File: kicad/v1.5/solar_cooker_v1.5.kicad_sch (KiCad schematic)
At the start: 18 parts, among them U10 GPS, U2 microSD, U3 clock_module, U5 anemometer, U6 BME680, U6 PT100, U7 pyranometer, U8 PT100, U9 AM2315, U9 PT100

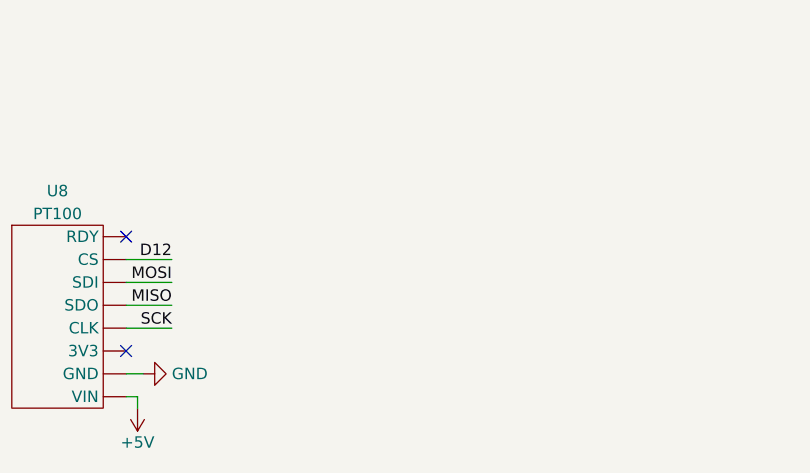
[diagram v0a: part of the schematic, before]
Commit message: added display
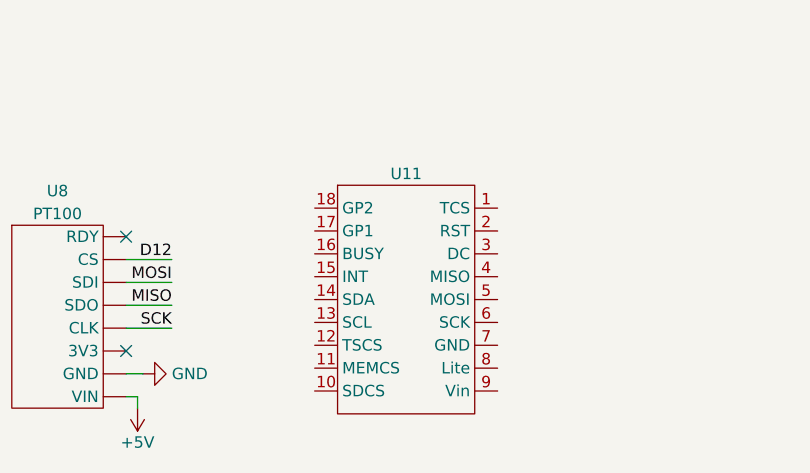
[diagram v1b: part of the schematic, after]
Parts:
- added U11: ~, custom_components:display, symbol custom_components:display
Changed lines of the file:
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@@
+    )
+  )
+  (symbol (lib_id "custom_components:display") (at 144.78 142.875 0) (unit 1)
+    (in_bom yes) (on_board yes) (dnp no) (fields_autoplaced)
+    (property "Reference" "U11" (at 144.78 142.875 0)
+      (effects (font (size 1.27 1.27)))
+    )
+    (property "Value" "~" (at 144.78 142.875 0)
+      (effects (font (size 1.27 1.27)))
+    )
+    (property "Footprint" "custom_components:display" (at 144.78 142.875 0)
+      (effects (font (size 1.27 1.27)) hide)
+    )
+    (property "Datasheet" "" (at 144.78 142.875 0)
+      (effects (font (size 1.27 1.27)) hide)
+    )
+    (pin "1")
+    (pin "10")
+    (pin "11")
+    (pin "12")
+    (pin "13")
+    (pin "14")
+    (pin "15")
+    (pin "16")
+    (pin "17")
+    (pin "18")
+    (pin "2")
+    (pin "3")
+    (pin "4")
+    (pin "5")
+    (pin "6")
+    (pin "7")
+    (pin "8")
+    (pin "9")
+    (instances
+      (project "solar_cooker_v1.5"
+        (path "/c2c342ae-c172-4b44-a50e-ddd387eb2591"
+          (reference "U11") (unit 1)
+        )
+      )
     )
   )

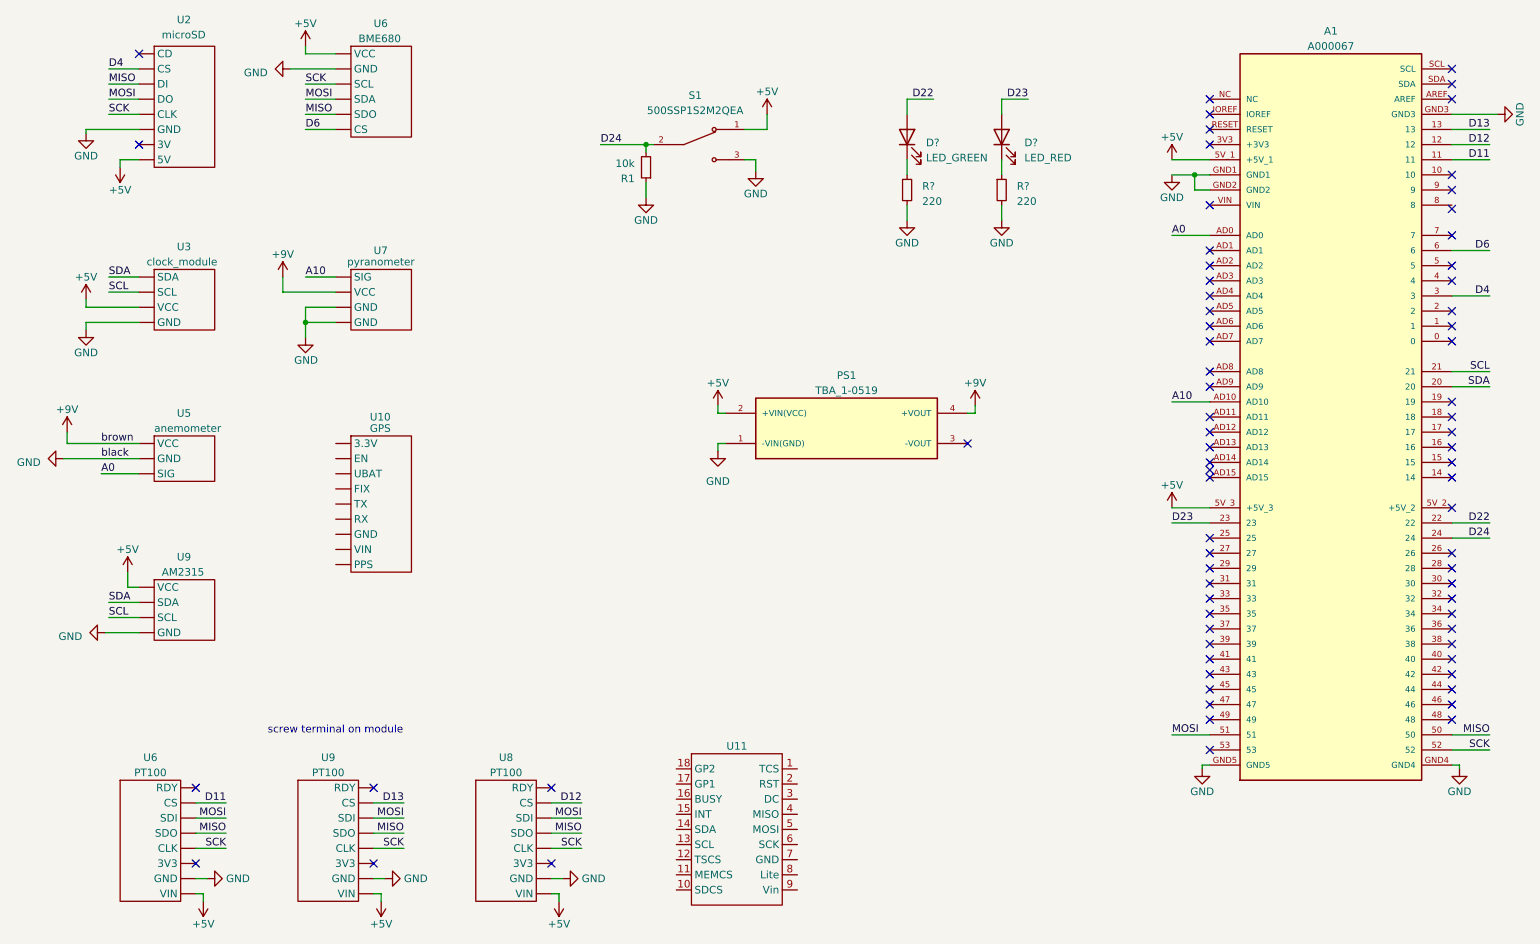
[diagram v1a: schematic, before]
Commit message: added display connections
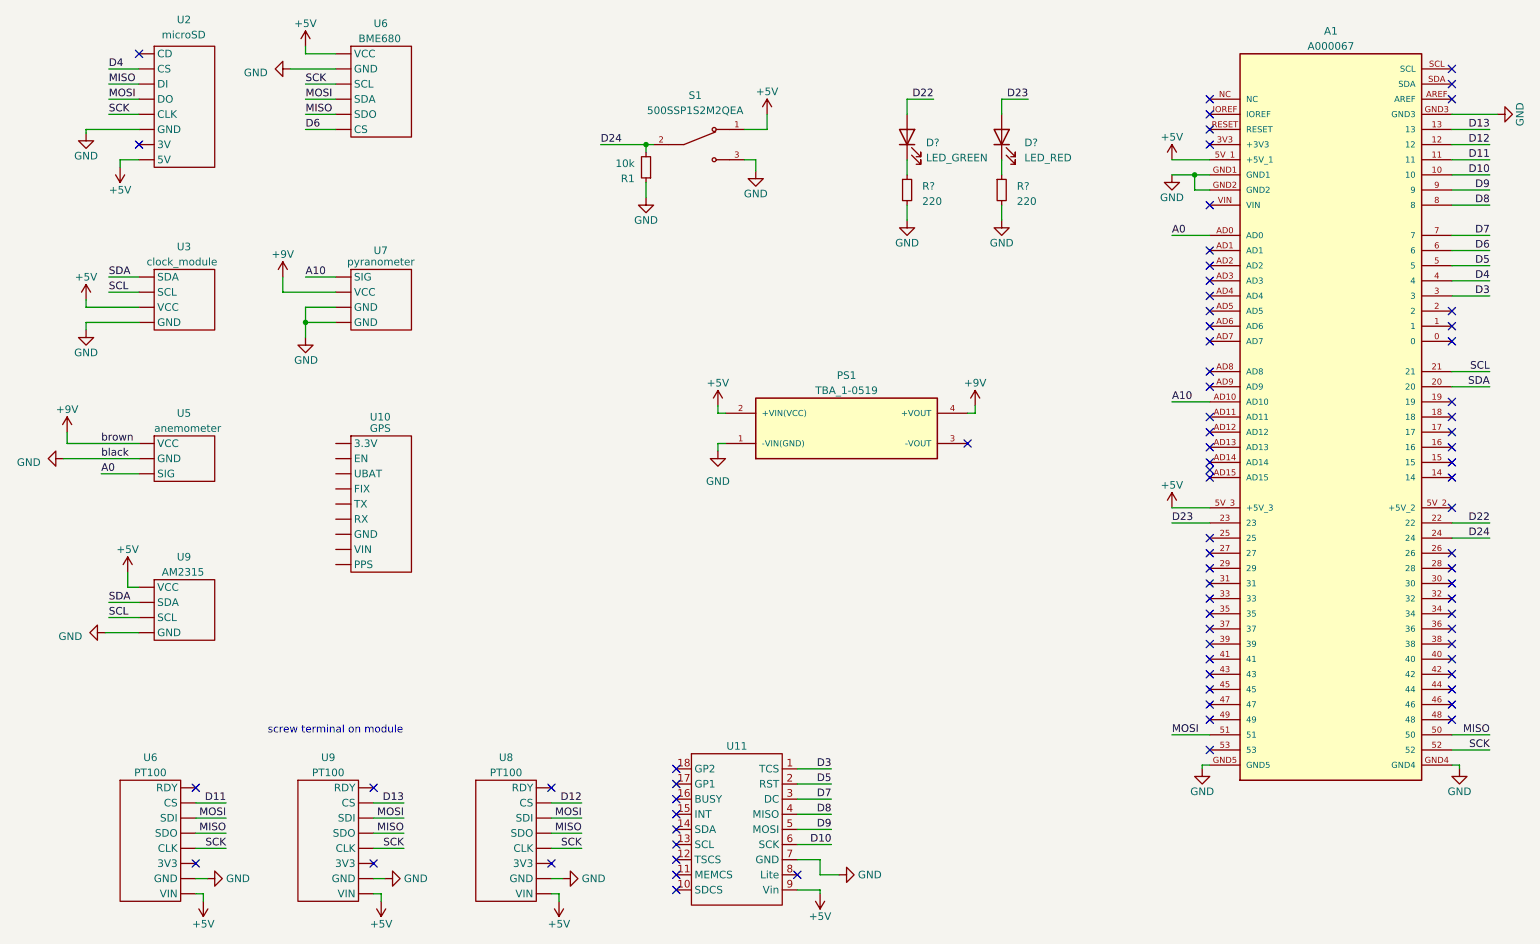
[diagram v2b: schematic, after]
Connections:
- net +5V: now also U11.9 (Vin)
- net D4: now also A1.4; no longer A1.3
- net GND: now also U11.7 (GND)
- net D3: now reaches U11.1 (TCS)
- net D3: now also A1.3
- net D5: now reaches U11.2 (RST)
- net D5: now also A1.5
- net D7: now reaches U11.3 (DC)
- net D7: now also A1.7
- net D8: now reaches U11.4 (MISO)
- net D8: now also A1.8
- net D9: now reaches U11.5 (MOSI)
- net D9: now also A1.9
- net D10: now reaches U11.6 (SCK)
- net D10: now also A1.10
- no-connect marks 74 -> 78

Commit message: updated display connections
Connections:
- net MISO: now also U11.4 (MISO)
- net MOSI: now also U11.5 (MOSI)
- net SCK: now also U11.6 (SCK)
- net D10: no longer names the net of A1.10
- net D10: no longer U11.6 (SCK)
- net D8: no longer names the net of A1.8
- net D8: no longer U11.4 (MISO)
- net D9: no longer names the net of A1.9
- net D9: no longer U11.5 (MOSI)
- no-connect marks 78 -> 81
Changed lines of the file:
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@@
   (no_connect (at 44.45 26.67))
   (no_connect (at 134.62 164.465))
+  (no_connect (at 264.795 46.99))
   (no_connect (at 264.795 69.85))
   (no_connect (at 224.155 82.55))
@@
   (no_connect (at 134.62 149.225))
   (no_connect (at 224.155 125.73))
+  (no_connect (at 264.795 52.07))
   (no_connect (at 264.795 92.71))
   (no_connect (at 183.515 92.075))
@@
   (no_connect (at 224.155 118.11))
   (no_connect (at 224.155 87.63))
+  (no_connect (at 264.795 49.53))
   (no_connect (at 224.155 138.43))
   (no_connect (at 83.82 149.86))
@@
     (stroke (width 0) (type default) (color 0 0 255 1))
   )
-  (wire (pts (xy 264.795 46.99) (xy 271.145 46.99))
-    (stroke (width 0) (type default))
-  )
   (wire (pts (xy 53.975 157.48) (xy 59.055 157.48))
     (stroke (width 0) (type default) (color 0 0 255 1))
@@
     (stroke (width 0) (type default))
   )
-  (wire (pts (xy 264.795 52.07) (xy 271.145 52.07))
-    (stroke (width 0) (type default))
-  )
   (wire (pts (xy 146.05 39.37) (xy 149.86 39.37))
     (stroke (width 0) (type default) (color 255 0 0 1))
@@
     (stroke (width 0) (type default) (color 255 0 0 1))
   )
+  (wire (pts (xy 154.94 156.845) (xy 160.655 156.845))
+    (stroke (width 0) (type default))
+  )
   (wire (pts (xy 39.37 31.75) (xy 44.45 31.75))
     (stroke (width 0) (type default) (color 0 0 255 1))
   )
-  (wire (pts (xy 264.795 49.53) (xy 271.145 49.53))
-    (stroke (width 0) (type default))
-  )
   (wire (pts (xy 154.94 151.765) (xy 160.655 151.765))
     (stroke (width 0) (type default))
@@
     (stroke (width 0) (type default))
   )
-  (wire (pts (xy 154.94 159.385) (xy 160.655 159.385))
+  (wire (pts (xy 154.94 159.385) (xy 161.925 159.385))
     (stroke (width 0) (type default))
   )
@@
     (stroke (width 0) (type default) (color 255 0 0 1))
   )
-  (wire (pts (xy 154.94 154.305) (xy 160.655 154.305))
+  (wire (pts (xy 154.94 154.305) (xy 162.56 154.305))
     (stroke (width 0) (type default))
   )
@@
   )
   (wire (pts (xy 217.805 105.41) (xy 224.155 105.41))
-    (stroke (width 0) (type default))
-  )
-  (wire (pts (xy 154.94 156.845) (xy 160.655 156.845))
     (stroke (width 0) (type default))
   )
@@
     (effects (font (size 1.27 1.27)) (justify right bottom))
   )
+  (label "SCK" (at 161.925 159.385 180) (fields_autoplaced)
+    (effects (font (size 1.27 1.27)) (justify right bottom))
+  )
   (label "D5" (at 160.655 149.225 180) (fields_autoplaced)
     (effects (font (size 1.27 1.27)) (justify right bottom))
   )
-  (label "D10" (at 271.145 46.99 180) (fields_autoplaced)
-    (effects (font (size 1.27 1.27)) (justify right bottom))
-  )
   (label "A0" (at 217.805 57.15 0) (fields_autoplaced)
     (effects (font (size 1.27 1.27)) (justify left bottom))
   )
-  (label "D8" (at 271.145 52.07 180) (fields_autoplaced)
-    (effects (font (size 1.27 1.27)) (justify right bottom))
-  )
   (label "D23" (at 193.675 34.29 180) (fields_autoplaced)
     (effects (font (size 1.27 1.27)) (justify right bottom))
@@
     (effects (font (size 1.27 1.27)) (justify right bottom))
   )
-  (label "D10" (at 160.655 159.385 180) (fields_autoplaced)
-    (effects (font (size 1.27 1.27)) (justify right bottom))
-  )
   (label "D24" (at 271.145 107.95 180) (fields_autoplaced)
     (effects (font (size 1.27 1.27)) (justify right bottom))
@@
     (effects (font (size 1.27 1.27)) (justify right bottom))
   )
-  (label "D8" (at 160.655 154.305 180) (fields_autoplaced)
-    (effects (font (size 1.27 1.27)) (justify right bottom))
-  )
   (label "brown" (at 38.1 92.075 0) (fields_autoplaced)
     (effects (font (size 1.27 1.27)) (justify left bottom))
@@
     (effects (font (size 1.27 1.27)) (justify left bottom))
   )
-  (label "D9" (at 271.145 49.53 180) (fields_autoplaced)
-    (effects (font (size 1.27 1.27)) (justify right bottom))
-  )
   (label "D6" (at 271.145 59.69 180) (fields_autoplaced)
     (effects (font (size 1.27 1.27)) (justify right bottom))
@@
     (effects (font (size 1.27 1.27)) (justify left bottom))
   )
+  (label "MISO" (at 162.56 154.305 180) (fields_autoplaced)
+    (effects (font (size 1.27 1.27)) (justify right bottom))
+  )
   (label "D7" (at 160.655 151.765 180) (fields_autoplaced)
     (effects (font (size 1.27 1.27)) (justify right bottom))
@@
     (effects (font (size 1.27 1.27)) (justify left bottom))
   )
-  (label "D9" (at 160.655 156.845 180) (fields_autoplaced)
-    (effects (font (size 1.27 1.27)) (justify right bottom))
+  (label "MOSI" (at 158.115 156.845 0) (fields_autoplaced)
+    (effects (font (size 1.27 1.27)) (justify left bottom))
   )
   (label "SCK" (at 72.39 31.75 0) (fields_autoplaced)
